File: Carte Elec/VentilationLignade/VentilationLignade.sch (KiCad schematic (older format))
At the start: 37 parts, among them P1 RelaisBoard1, P10 SDCard, P11 Codeur Rotatif, P12 Teensy Bottom, P13 EndStops1, P14 Teensy_Haut, P15 EndStops2, P16 Teensy_cote, P17 Retour 12V, P18 Masse_12V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

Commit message: Reprise de carte  : Suppression MAX232, pour avoir la place de mettre les MOC207
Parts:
- removed C4, C5, C7, C8: C, ~, symbol C
- removed R2, R3: R, ~, symbol R
- removed U1: MAX232, symbol MAX232
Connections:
- wire segments 245 -> 216
- no-connect marks 13 -> 12
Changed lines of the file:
@@
 Sheet 1 2
 Title ""
-Date "9 sep 2015"
+Date "12 sep 2015"
 Rev ""
 Comp ""
@@
 	7950 4700 8200 4700
 $Comp
-L MAX232 U1
-U 1 1 55EEB4F2
-P 1800 4800
-F 0 "U1" H 1800 5650 70  0000 C CNN
-F 1 "MAX232" H 1800 3950 70  0000 C CNN
-F 2 "" H 1800 4800 60  0000 C CNN
-F 3 "" H 1800 4800 60  0000 C CNN
-	1    1800 4800
-	-1   0    0    -1
-$EndComp
-$Comp
-L C C7
-U 1 1 55EEB60C
-P 2800 4300
-F 0 "C7" H 2800 4400 40  0000 L CNN
-F 1 "C" H 2806 4215 40  0000 L CNN
-F 2 "~" H 2838 4150 30  0000 C CNN
-F 3 "~" H 2800 4300 60  0000 C CNN
-	1    2800 4300
-	1    0    0    -1
-$EndComp
-$Comp
-L C C8
-U 1 1 55EEB61B
-P 2800 4800
-F 0 "C8" H 2800 4900 40  0000 L CNN
-F 1 "C" H 2806 4715 40  0000 L CNN
-F 2 "~" H 2838 4650 30  0000 C CNN
-F 3 "~" H 2800 4800 60  0000 C CNN
-	1    2800 4800
-	1    0    0    -1
-$EndComp
-$Comp
 L CONN_4 P23
 U 1 1 55EEB62A
@@
 	-1   0    0    1
 $EndComp
-Wire Wire Line
-	2600 4100 2800 4100
-Wire Wire Line
-	2600 4500 2800 4500
-Wire Wire Line
-	2600 4600 2800 4600
-Wire Wire Line
-	2800 5000 2600 5000
-$Comp
-L GND #PWR038
-U 1 1 55EEBF63
-P 800 4750
-F 0 "#PWR038" H 800 4750 30  0001 C CNN
-F 1 "GND" H 800 4680 30  0001 C CNN
-F 2 "" H 800 4750 60  0000 C CNN
-F 3 "" H 800 4750 60  0000 C CNN
-	1    800  4750
-	1    0    0    -1
-$EndComp
-Wire Wire Line
-	800  4750 800  4700
-Wire Wire Line
-	800  4700 1000 4700
-$Comp
-L +3.3V #PWR039
-U 1 1 55EEC091
-P 800 4050
-F 0 "#PWR039" H 800 4010 30  0001 C CNN
-F 1 "+3.3V" H 800 4160 30  0000 C CNN
-F 2 "" H 800 4050 60  0000 C CNN
-F 3 "" H 800 4050 60  0000 C CNN
-	1    800  4050
-	1    0    0    -1
-$EndComp
-Wire Wire Line
-	800  4100 800  4050
-Wire Wire Line
-	550  4100 1000 4100
-$Comp
-L C C4
-U 1 1 55EF1C37
-P 550 4300
-F 0 "C4" H 550 4400 40  0000 L CNN
-F 1 "C" H 556 4215 40  0000 L CNN
-F 2 "~" H 588 4150 30  0000 C CNN
-F 3 "~" H 550 4300 60  0000 C CNN
-	1    550  4300
-	1    0    0    -1
-$EndComp
-$Comp
-L C C5
-U 1 1 55EF1C46
-P 550 4800
-F 0 "C5" H 550 4900 40  0000 L CNN
-F 1 "C" H 556 4715 40  0000 L CNN
-F 2 "~" H 588 4650 30  0000 C CNN
-F 3 "~" H 550 4800 60  0000 C CNN
-	1    550  4800
-	1    0    0    -1
-$EndComp
-Connection ~ 800  4100
-Wire Wire Line
-	550  4500 550  4600
-Wire Wire Line
-	550  5000 1000 5000
-$Comp
-L GND #PWR040
-U 1 1 55EF2234
-P 650 4600
-F 0 "#PWR040" H 650 4600 30  0001 C CNN
-F 1 "GND" H 650 4530 30  0001 C CNN
-F 2 "" H 650 4600 60  0000 C CNN
-F 3 "" H 650 4600 60  0000 C CNN
-	1    650  4600
-	1    0    0    -1
-$EndComp
-Wire Wire Line
-	550  4550 650  4550
-Wire Wire Line
-	650  4550 650  4600
-Connection ~ 550  4550
-$Comp
-L GND #PWR041
-U 1 1 55EF236C
-P 1700 5800
-F 0 "#PWR041" H 1700 5800 30  0001 C CNN
-F 1 "GND" H 1700 5730 30  0001 C CNN
-F 2 "" H 1700 5800 60  0000 C CNN
-F 3 "" H 1700 5800 60  0000 C CNN
-	1    1700 5800
-	1    0    0    -1
-$EndComp
-$Comp
-L R R2
-U 1 1 55EF237B
-P 1300 5700
-F 0 "R2" V 1380 5700 40  0000 C CNN
-F 1 "R" V 1307 5701 40  0000 C CNN
-F 2 "~" V 1230 5700 30  0000 C CNN
-F 3 "~" H 1300 5700 30  0000 C CNN
-	1    1300 5700
-	0    -1   -1   0
-$EndComp
-Wire Wire Line
-	950  5700 1050 5700
-Wire Wire Line
-	1550 5700 1700 5700
-Wire Wire Line
-	1700 5700 1700 5800
-$Comp
-L R R3
-U 1 1 55EF267E
-P 3000 5550
-F 0 "R3" V 3080 5550 40  0000 C CNN
-F 1 "R" V 3007 5551 40  0000 C CNN
-F 2 "~" V 2930 5550 30  0000 C CNN
-F 3 "~" H 3000 5550 30  0000 C CNN
-	1    3000 5550
-	1    0    0    -1
-$EndComp
-NoConn ~ 2600 5500
-Wire Wire Line
-	2600 5300 3000 5300
-$Comp
-L GND #PWR042
-U 1 1 55EF27BC
-P 3000 5850
-F 0 "#PWR042" H 3000 5850 30  0001 C CNN
-F 1 "GND" H 3000 5780 30  0001 C CNN
-F 2 "" H 3000 5850 60  0000 C CNN
-F 3 "" H 3000 5850 60  0000 C CNN
-	1    3000 5850
-	1    0    0    -1
-$EndComp
-Wire Wire Line
-	3000 5850 3000 5800
-Text GLabel 2750 5200 2    60   Input ~ 0
-TX
-Wire Wire Line
-	2750 5200 2600 5200
-Text GLabel 2750 5400 2    60   Output ~ 0
-RX
-Wire Wire Line
-	2750 5400 2600 5400
 Text GLabel 4300 6150 0    60   Input ~ 0
 RX
@@
 Connection ~ 1350 2350
 $Comp
-L +5V #PWR045
-U 1 1 55F02361
-P 800 4350
-F 0 "#PWR045" H 800 4440 20  0001 C CNN
-F 1 "+5V" H 800 4440 30  0000 C CNN
-F 2 "" H 800 4350 60  0000 C CNN
-F 3 "" H 800 4350 60  0000 C CNN
-	1    800  4350
-	1    0    0    -1
-$EndComp
-Wire Wire Line
-	800  4350 800  4500
-Wire Wire Line
-	800  5300 850  5300
-Wire Wire Line
-	850  5300 850  5500
-Wire Wire Line
-	850  5500 1000 5500
-Wire Wire Line
-	1000 5400 950  5400
-Wire Wire Line
-	950  5400 950  5700
-Wire Wire Line
-	950  5550 800  5550
-Wire Wire Line
-	800  5550 800  5500
-Wire Wire Line
-	1000 5300 950  5300
-Wire Wire Line
-	950  5300 950  5200
-Wire Wire Line
-	950  5200 800  5200
-Wire Wire Line
-	1000 5200 1000 5250
-Wire Wire Line
-	1000 5250 900  5250
-Wire Wire Line
-	900  5250 900  5400
-Wire Wire Line
-	900  5400 800  5400
-Connection ~ 950  5550
-Wire Wire Line
-	800  4500 1000 4500
-$Comp
 L CONN_10 P12
 U 1 1 55F0328C
@@
 NoConn ~ 5200 5400
 NoConn ~ 5300 5400
+$Comp
+L +5V #PWR?
+U 1 1 55F44B6E
+P 950 5100
+F 0 "#PWR?" H 950 5190 20  0001 C CNN
+F 1 "+5V" H 950 5190 30  0000 C CNN
+F 2 "" H 950 5100 60  0000 C CNN
+F 3 "" H 950 5100 60  0000 C CNN
+	1    950  5100
+	1    0    0    -1
+$EndComp
+$Comp
+L GND #PWR?
+U 1 1 55F44B7D
+P 950 5600
+F 0 "#PWR?" H 950 5600 30  0001 C CNN
+F 1 "GND" H 950 5530 30  0001 C CNN
+F 2 "" H 950 5600 60  0000 C CNN
+F 3 "" H 950 5600 60  0000 C CNN
+	1    950  5600
+	1    0    0    -1
+$EndComp
+Text GLabel 950  5300 2    60   Input ~ 0
+RX
+Text GLabel 950  5400 2    60   Output ~ 0
+TX
+Wire Wire Line
+	800  5200 950  5200
+Wire Wire Line
+	950  5200 950  5100
+Wire Wire Line
+	800  5300 950  5300
+Wire Wire Line
+	800  5400 950  5400
+Wire Wire Line
+	800  5500 950  5500
+Wire Wire Line
+	950  5500 950  5600
 $EndSCHEMATC

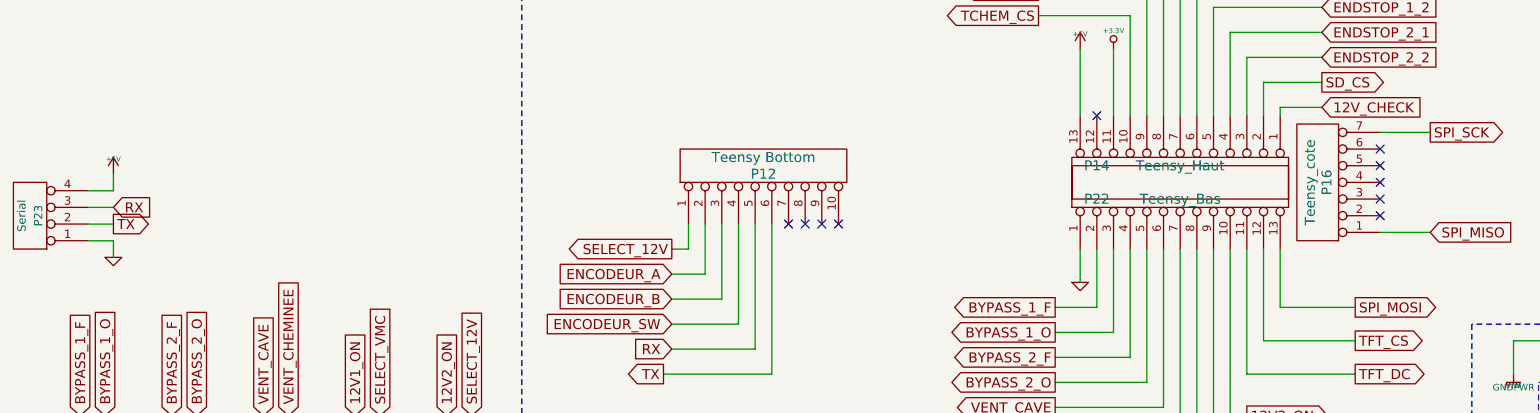
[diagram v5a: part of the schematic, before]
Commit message: Changement taille 100x160 (pour fab maison)
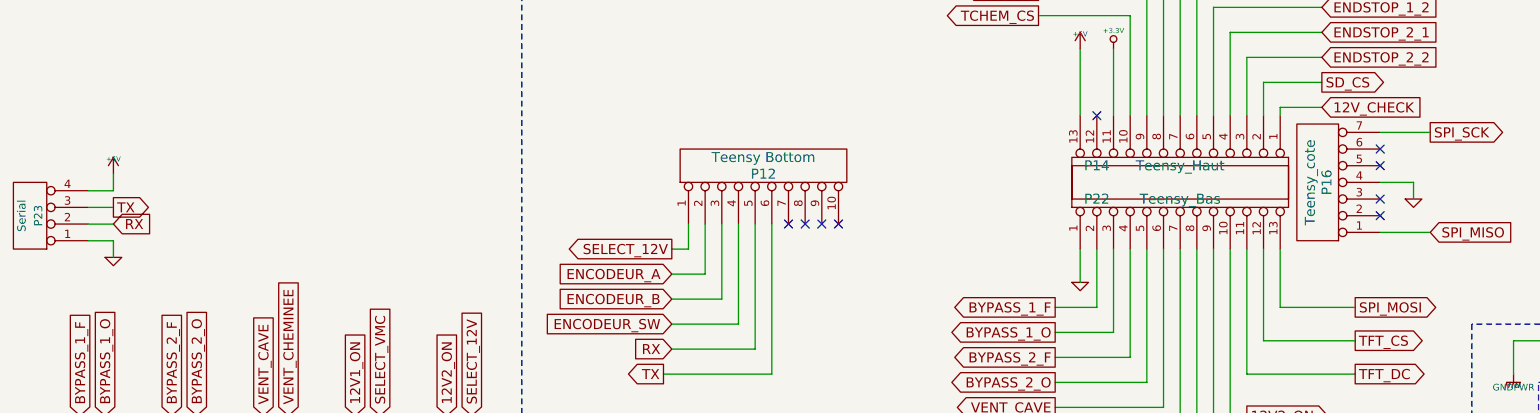
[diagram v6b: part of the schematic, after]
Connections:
- net GND: now also P16.4 (P4)
- net RX: now also P23.2 (P2); no longer P23.3 (P3)
- net TX: now also P23.3 (P3); no longer P23.2 (P2)
- no-connect marks 12 -> 11
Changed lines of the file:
@@
 Sheet 1 2
 Title ""
-Date "12 sep 2015"
+Date "13 sep 2015"
 Rev ""
 Comp ""
@@
 NoConn ~ 8550 5350
 NoConn ~ 8550 5250
-NoConn ~ 8550 5150
 NoConn ~ 8550 5050
 NoConn ~ 8550 4950
@@
 	1    0    0    -1
 $EndComp
-Text GLabel 950  5300 2    60   Input ~ 0
+Text GLabel 950  5400 2    60   Input ~ 0
 RX
-Text GLabel 950  5400 2    60   Output ~ 0
+Text GLabel 950  5300 2    60   Output ~ 0
 TX
 Wire Wire Line
@@
 Wire Wire Line
 	950  5500 950  5600
+$Comp
+L GND #PWR?
+U 1 1 55F5D525
+P 8750 5250
+F 0 "#PWR?" H 8750 5250 30  0001 C CNN
+F 1 "GND" H 8750 5180 30  0001 C CNN
+F 2 "" H 8750 5250 60  0000 C CNN
+F 3 "" H 8750 5250 60  0000 C CNN
+	1    8750 5250
+	1    0    0    -1
+$EndComp
+Wire Wire Line
+	8750 5250 8750 5150
+Wire Wire Line
+	8750 5150 8550 5150
 $EndSCHEMATC

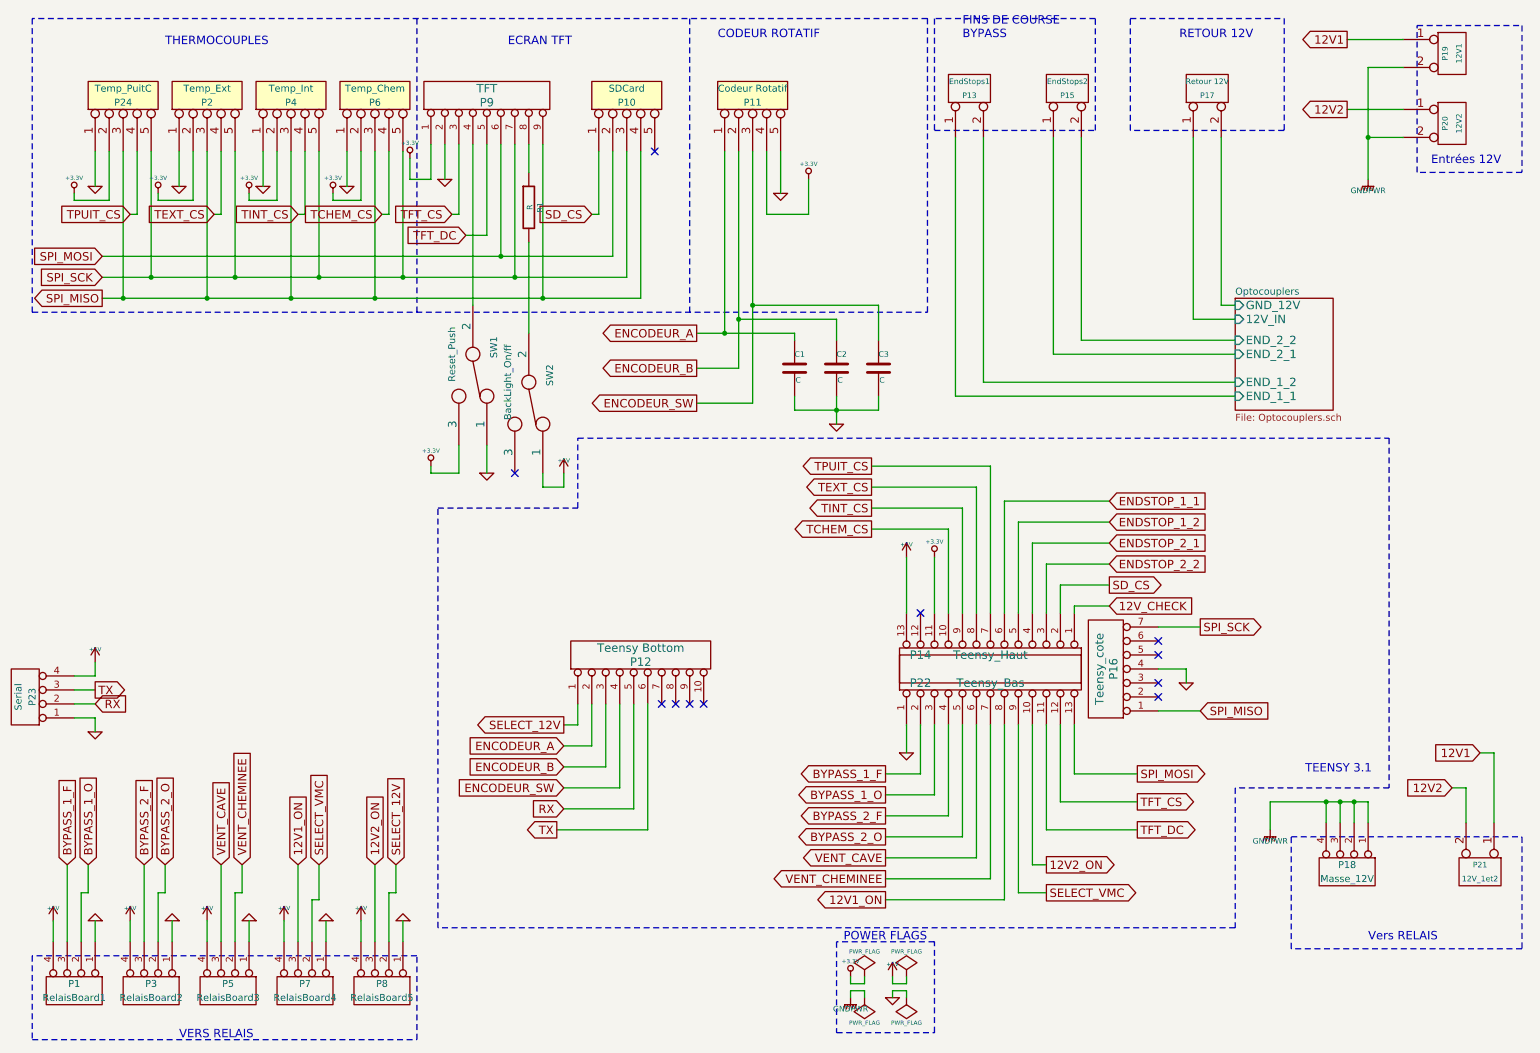
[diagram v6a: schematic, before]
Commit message: Modification carte pour utiliser thermistors et real time clock.
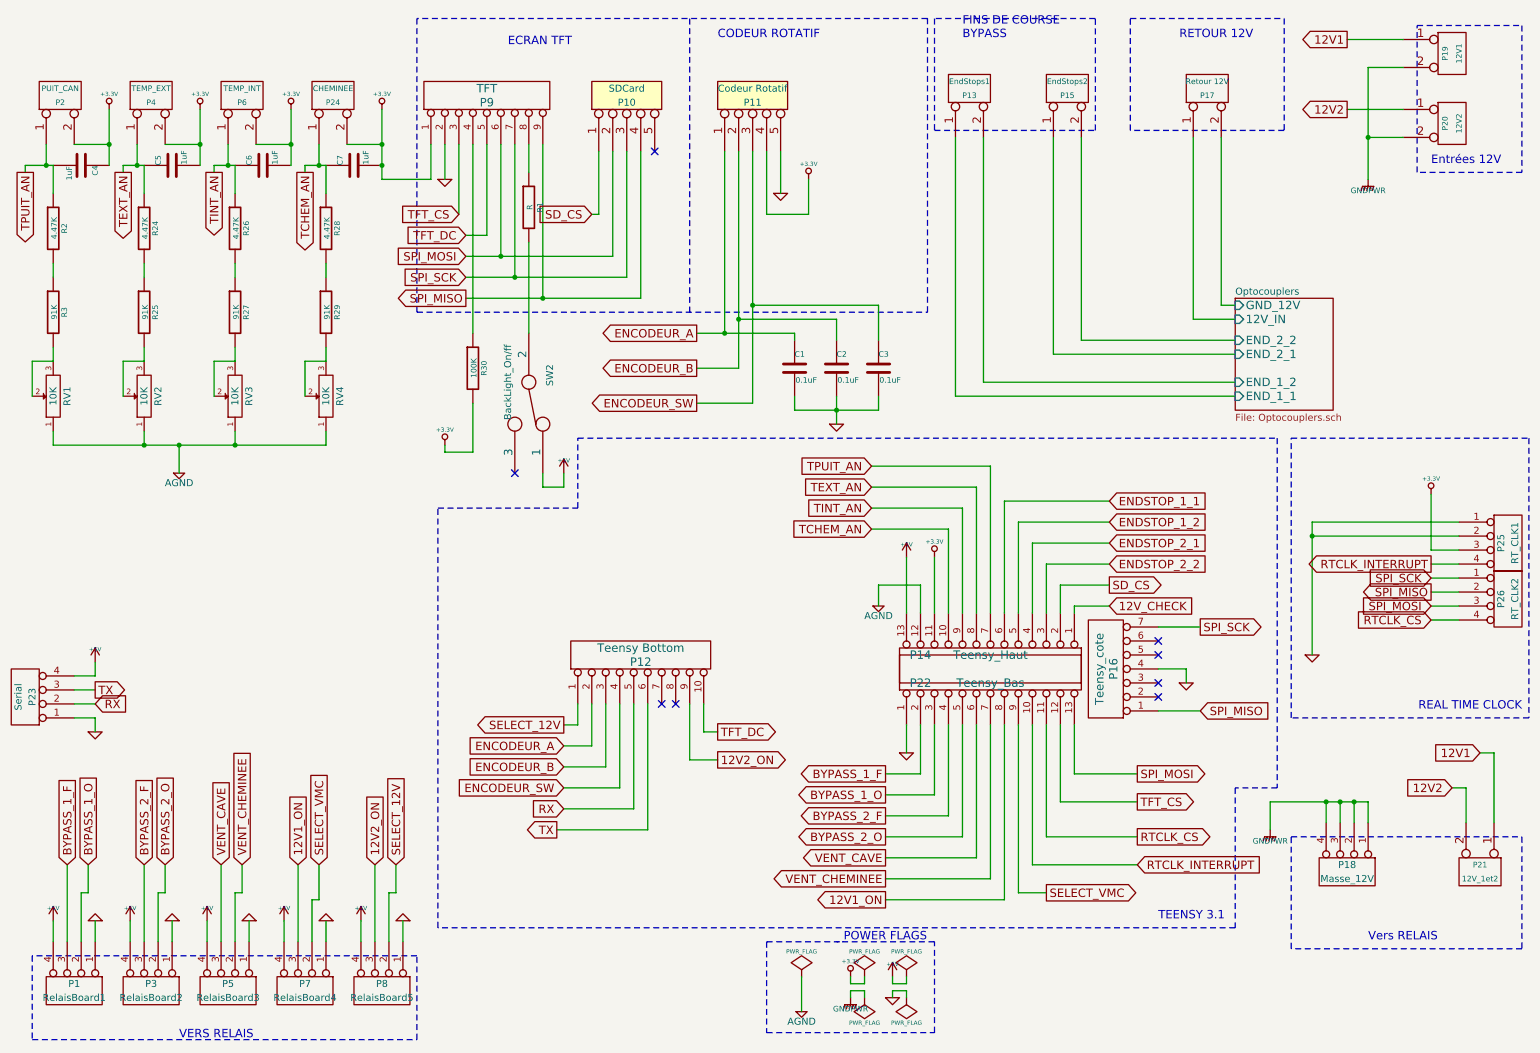
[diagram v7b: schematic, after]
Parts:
- removed P2: Temp_Ext, symbol CONN_5
- removed P24: Temp_PuitC, symbol CONN_5
- removed P4: Temp_Int, symbol CONN_5
- removed P6: Temp_Chem, symbol CONN_5
- removed SW1: Reset_Push, ~, symbol SWITCH_INV
- added C4, C5, C6, C7: 1uF, ~, symbol C
- added P2: PUIT_CAN, symbol CONN_2
- added P24: CHEMINEE, symbol CONN_2
- added P25: RT_CLK1, symbol CONN_4
- added P26: RT_CLK2, symbol CONN_4
- added P4: TEMP_EXT, symbol CONN_2
- added P6: TEMP_INT, symbol CONN_2
- added R2, R24, R26, R28: 4.47K, ~, symbol R
- added R25, R27, R29, R3: 91K, ~, symbol R
- added R30: 100K, ~, symbol R
- added RV1, RV2, RV3, RV4: 10K, ~, symbol POT
- C1, C2, C3: value C -> 0.1uF
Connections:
- net +3.3V: now also C4.1, C5.2, C6.2, C7.2, P2.2 (PM), P24.2 (PM), P25.3 (P3), P4.2 (PM), P6.2 (PM), R30.2
- net 12V2_ON: now also P12.9 (P9); no longer P22.10 (P10)
- net GND: now also P25.1 (P1), P25.2 (P2)
- net SPI_MISO: now also P26.2 (P2)
- net SPI_MOSI: now also P26.3 (P3)
- net SPI_SCK: now also P26.1 (P1)
- net TFT_DC: now also P12.10 (P10); no longer P22.11 (P11)
- net at P9.4 (P4): now also R30.1
- net AGND: now reaches P14.12 (P12)
- net AGND: now also RV1.1, RV2.1, RV3.1, RV4.1
- net TCHEM_CS renamed TCHEM_AN
- net TCHEM_AN: now also C7.1, P24.1 (P1), R28.1
- net TEXT_CS renamed TEXT_AN
- net TEXT_AN: now also C5.1, P4.1 (P1), R24.1
- net TINT_CS renamed TINT_AN
- net TINT_AN: now also C6.1, P6.1 (P1), R26.1
- net TPUIT_CS renamed TPUIT_AN
- net TPUIT_AN: now also C4.2, P2.1 (P1), R2.1
- new net: R2.2, R3.1
- new net: R3.2, RV1.2, RV1.3
- new net: R24.2, R25.1
- new net: R25.2, RV2.2, RV2.3
- new net: R26.2, R27.1
- new net: R27.2, RV3.2, RV3.3
- new net: R28.2, R29.1
- new net: R29.2, RV4.2, RV4.3
- new net RTCLK_CS: P22.11 (P11), P26.4 (P4)
- new net RTCLK_INTERRUPT: P22.10 (P10), P25.4 (P4)
- no-connect marks 11 -> 8
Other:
- note added: "REAL TIME CLOCK"
- note removed: "THERMOCOUPLES"

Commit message: Changement des boitiers en cours de reroutage
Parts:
- C1, C2, C3: footprint ~ -> Capacitors_ThroughHole:C_Rect_L7_W2.5_P5; symbol C -> C-RESCUE-VentilationLignade
- C4, C5, C6, C7: footprint ~ -> Capacitors_ThroughHole:C_Radial_D8_L11.5_P3.5; symbol C -> C-RESCUE-VentilationLignade
- P1, P18, P23, P25, P26, P3, P5, P7, P8: footprint (none) -> Pin_Headers:Pin_Header_Straight_1x04
- P10, P11: footprint (none) -> Pin_Headers:Pin_Header_Straight_1x05
- P12: footprint (none) -> Pin_Headers:Pin_Header_Straight_1x10
- P13, P15, P17, P19, P2, P20, P21, P24, P4, P6: footprint (none) -> Connect:bornier2
- P14, P22: footprint (none) -> Pin_Headers:Pin_Header_Straight_1x13
- P16: footprint (none) -> Pin_Headers:Pin_Header_Straight_1x07
- P9: footprint (none) -> Pin_Headers:Pin_Header_Straight_1x09
- R1: footprint ~ -> Resistors_ThroughHole:Resistor_Horizontal_RM15mm; symbol R -> R-RESCUE-VentilationLignade
- R2, R24, R25, R26, R27, R28, R29, R3, R30: footprint ~ -> Resistors_SMD:R_1206_HandSoldering; symbol R -> R-RESCUE-VentilationLignade
- RV1, RV2, RV3, RV4: footprint ~ -> Potentiometers:Potentiometer_Bourns_3339S_Angular_ScrewFront
- SW2: footprint ~ -> Pin_Headers:Pin_Header_Straight_1x03
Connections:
- net +3.3V: now also C4.2, P2.1 (P1), P24.1 (P1), P4.1 (P1), P6.1 (P1); no longer C4.1, P2.2 (PM), P24.2 (PM), P4.2 (PM), P6.2 (PM)
- net Optocouplers/12V_IN: now also P17.2 (PM); no longer P17.1 (P1)
- net Optocouplers/END_1_1: now also P13.2 (PM); no longer P13.1 (P1)
- net Optocouplers/END_1_2: now also P13.1 (P1); no longer P13.2 (PM)
- net Optocouplers/END_2_1: now also P15.2 (PM); no longer P15.1 (P1)
- net Optocouplers/END_2_2: now also P15.1 (P1); no longer P15.2 (PM)
- net Optocouplers/GND_12V: now also P17.1 (P1); no longer P17.2 (PM)
- net TCHEM_AN: now also P24.2 (PM); no longer P24.1 (P1)
- net TEXT_AN: now also P4.2 (PM); no longer P4.1 (P1)
- net TINT_AN: now also P14.7 (P7), P6.2 (PM); no longer P14.9 (P9), P6.1 (P1)
- net TPUIT_AN: now also C4.1, P14.9 (P9), P2.2 (PM); no longer C4.2, P14.7 (P7), P2.1 (P1)
